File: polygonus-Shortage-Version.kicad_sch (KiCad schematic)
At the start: 10 parts, among them J1 Conn_01x01, J2 Conn_01x01, J3 Conn_01x01, J4 Conn_01x32, J5 Conn_01x32, J6 Conn_01x16, J7 Conn_01x16

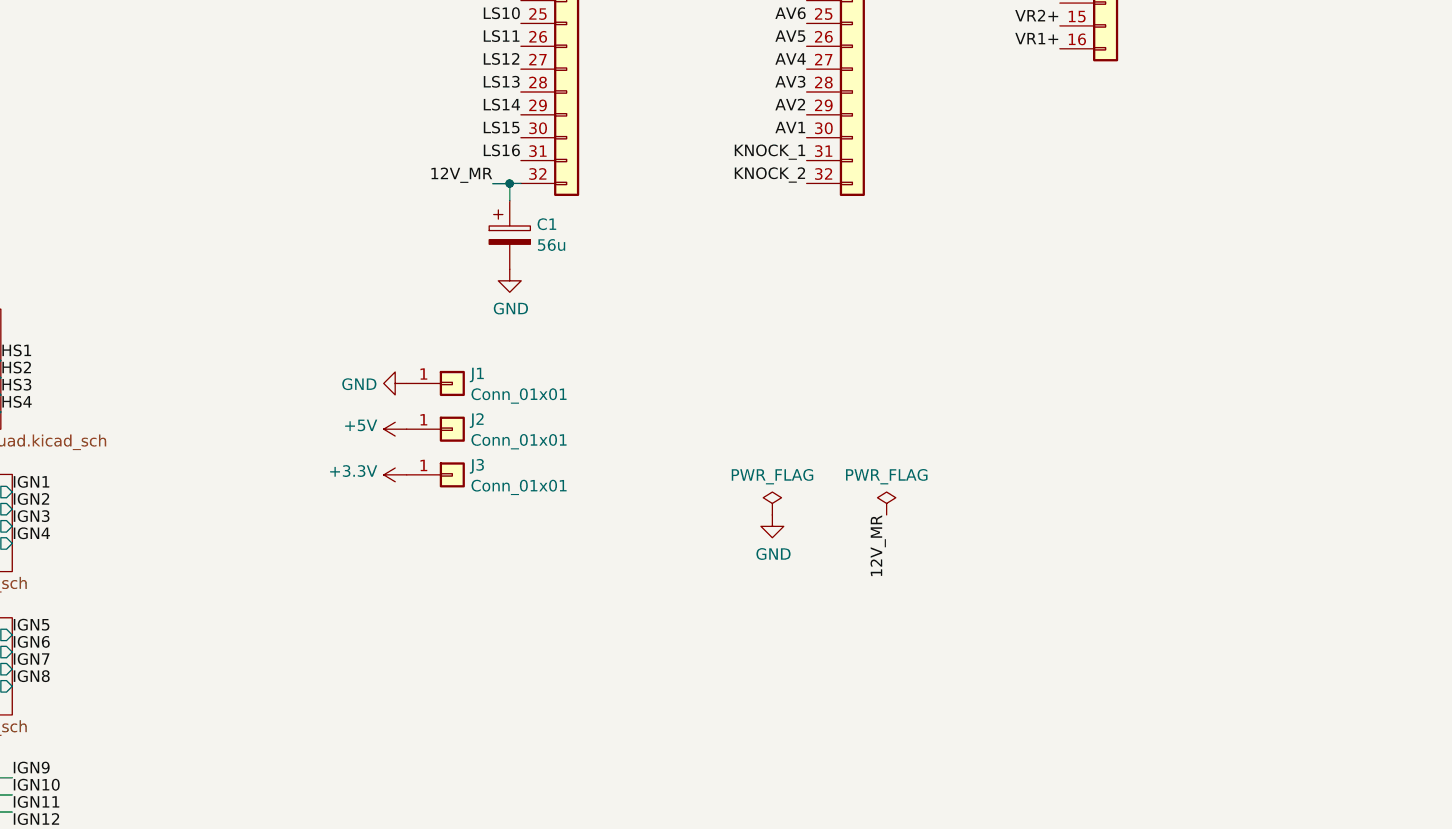
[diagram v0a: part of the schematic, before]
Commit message: added 12v notes to schematic
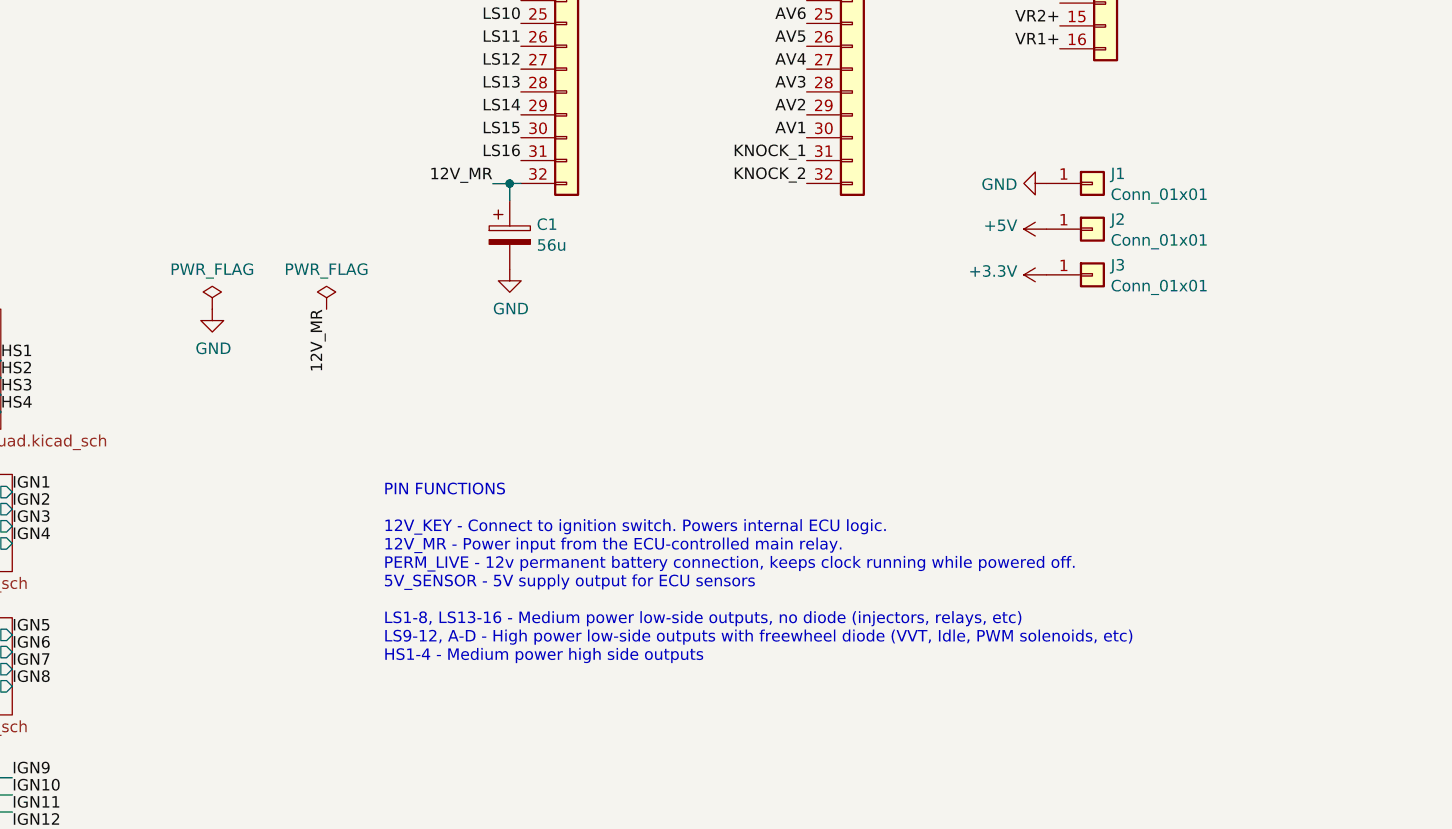
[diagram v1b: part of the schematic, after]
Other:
- note added: "PIN FUNCTIONS 12V_KEY - Connect to ignition switch. Powers internal ECU logic. 12V_MR - Power input from the ECU-controlled main relay. PERM_LIVE - 12v permanent battery connection, keeps clock running while powered off. 5V_SENSOR - 5V supply output for ECU sensors LS1-8, LS13-16 - Medium power low-side outputs, no diode (injectors, relays, etc) LS9-12, A-D - High power low-side outputs with free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"
- moved on the sheet: J1, J2, J3

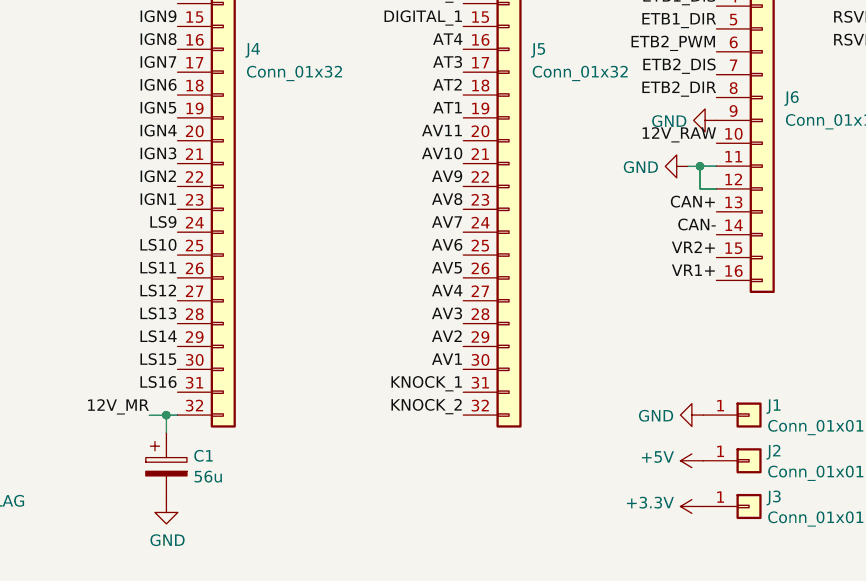
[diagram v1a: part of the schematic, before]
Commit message: Published 1.5 gerbs, bom, cpl and pdf
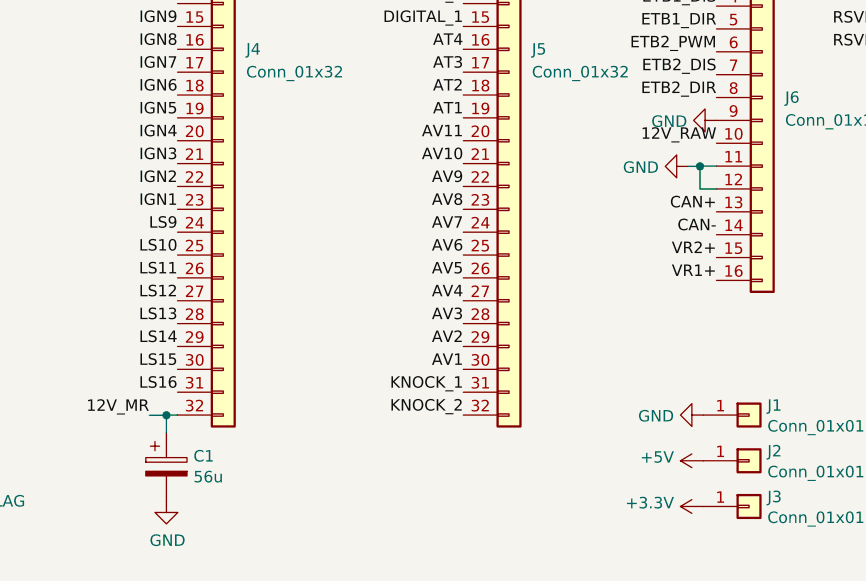
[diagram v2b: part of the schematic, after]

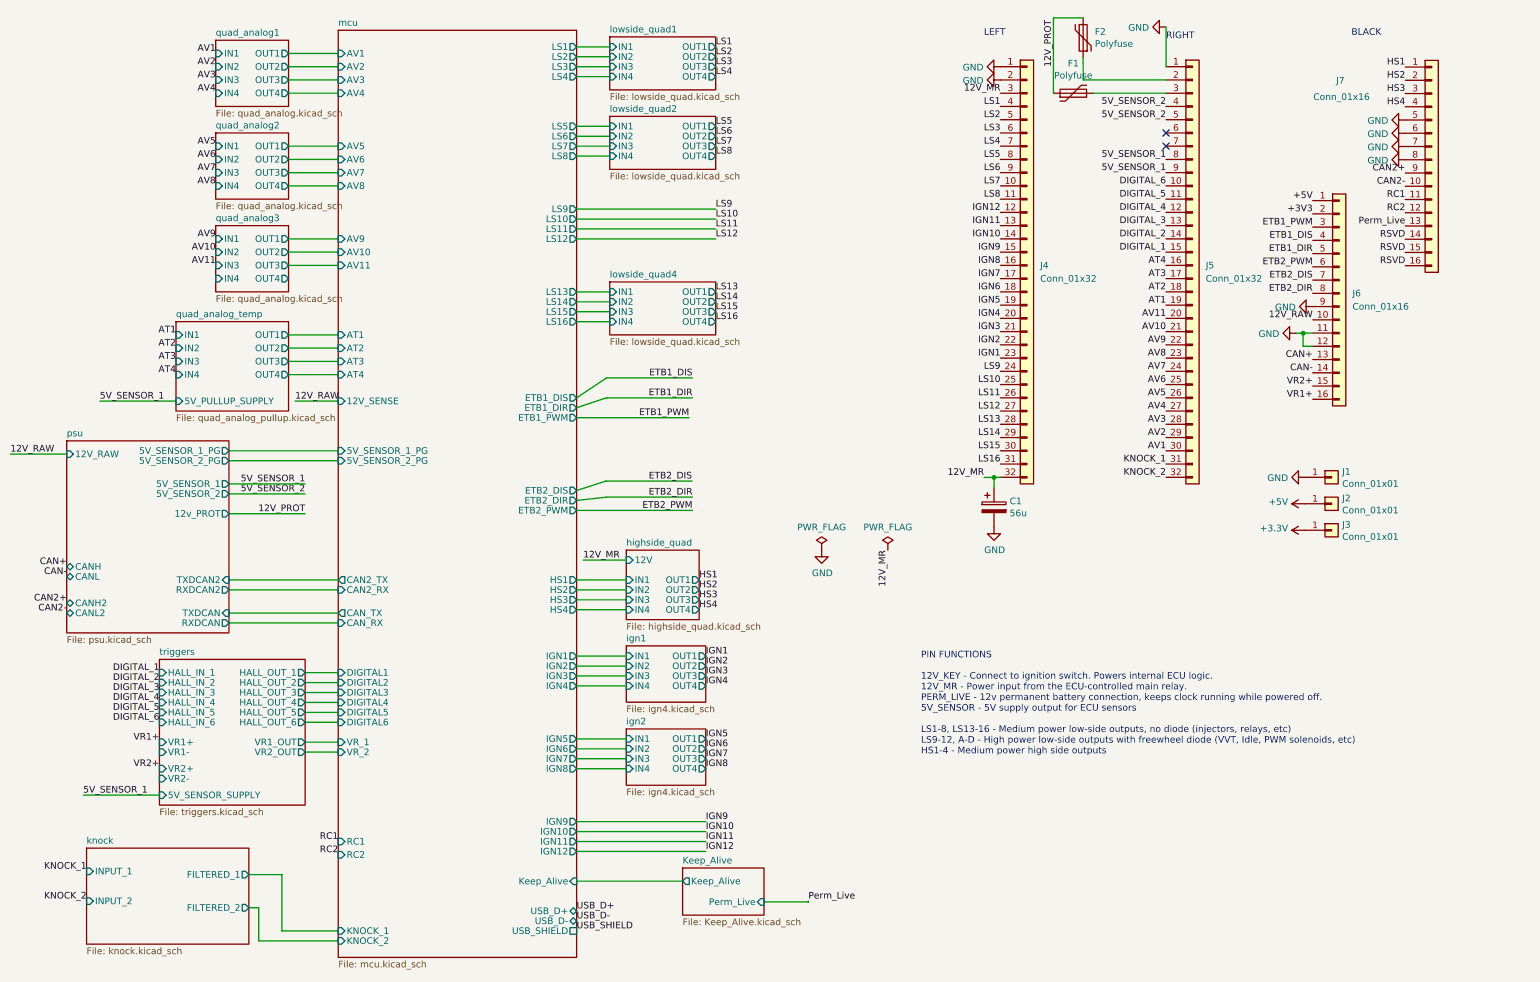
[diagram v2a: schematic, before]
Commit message: make hardware updates: - fix erc/drc errors - switch to VNLD5090 - switch to SOIC8 ignition drivers - BOM deduplication of similar parts
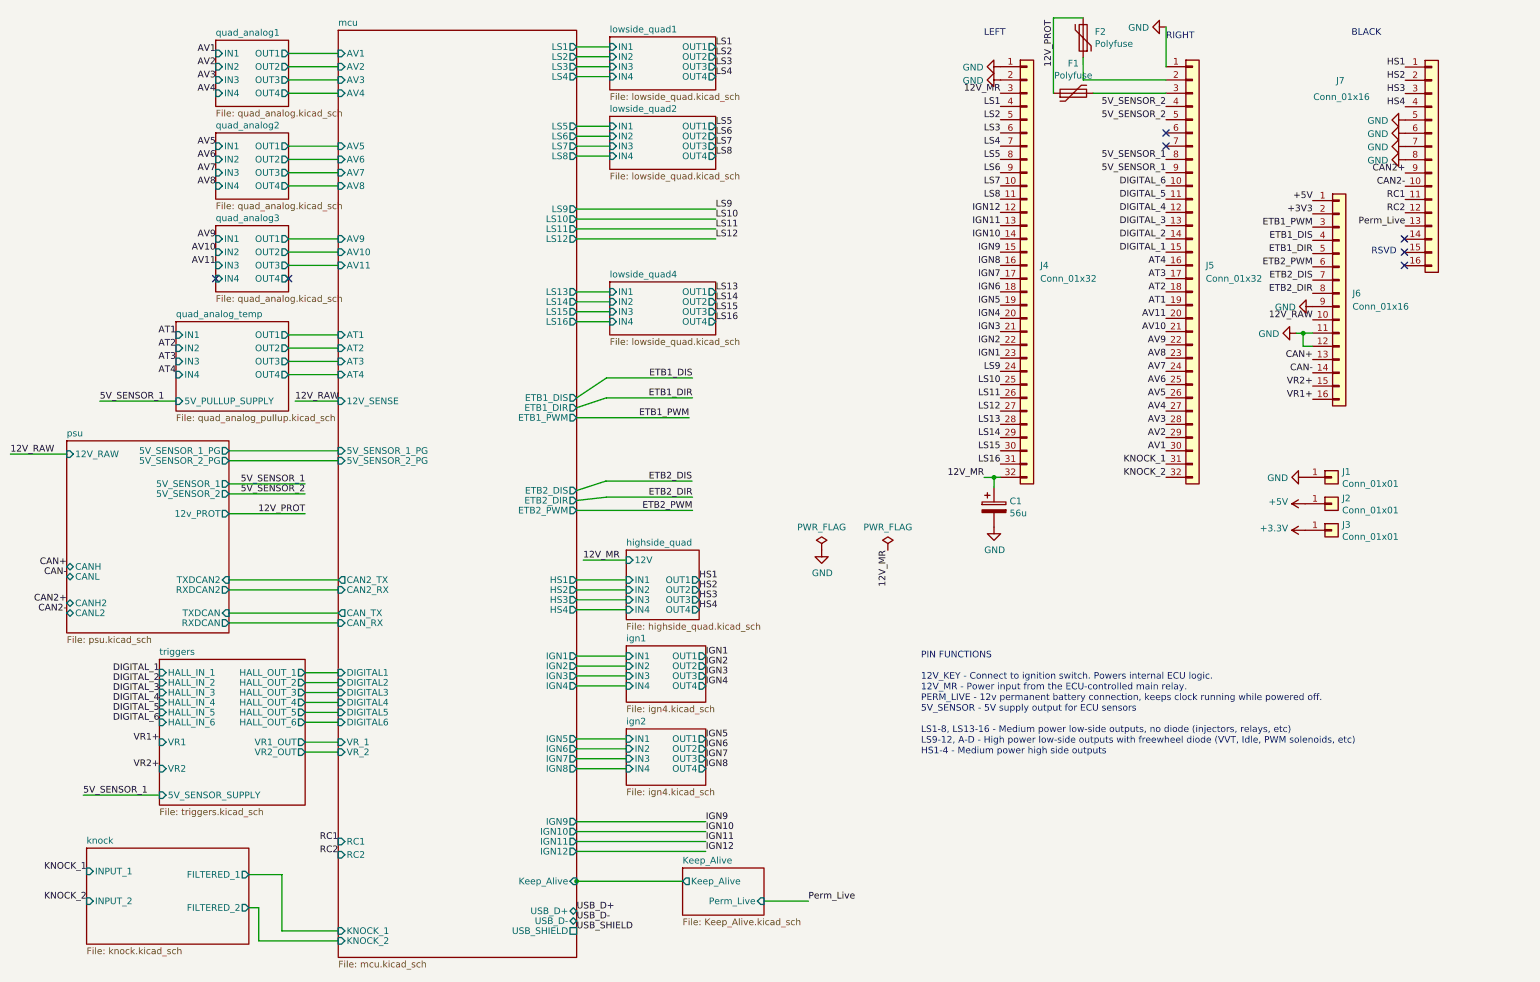
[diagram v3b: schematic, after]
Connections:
- removed net RSVD: J7.14 (Pin_14), J7.15 (Pin_15), J7.16 (Pin_16)
- no-connect marks 2 -> 7
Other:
- sheet triggers ports: added VR1, VR2; removed VR1+, VR1-, VR2+, VR2-
- note added: "RSVD"
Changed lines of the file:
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@@
   (junction (at 253.6325 75.2399) (diameter 0) (color 0 0 0 0)
   )
+  (junction (at 114.3 180.34) (diameter 0) (color 0 0 0 0)
+  )
+  (no_connect (at 45.085 64.77))
+  (no_connect (at 59.055 64.77))
+  (no_connect (at 273.05 59.69))
   (no_connect (at 227.33 36.83))
   (no_connect (at 227.33 39.37))
+  (no_connect (at 273.05 62.23))
+  (no_connect (at 273.05 57.15))
   (wire (pts (xy 62.23 144.145) (xy 68.58 144.145))
     (stroke (width 0) (type default))
   )
-  (wire (pts (xy 150.2316 184.3116) (xy 158.75 184.3116))
+  (wire (pts (xy 150.2316 184.15) (xy 158.75 184.15))
     (stroke (width 0) (type default))
   )
@@
     (stroke (width 0) (type default))
   )
-  (wire (pts (xy 134.62 180.325) (xy 114.3 180.325))
-    (stroke (width 0) (type default))
-  )
   (wire (pts (xy 68.58 59.69) (xy 59.055 59.69))
     (stroke (width 0) (type default))
@@
     (stroke (width 0) (type default))
   )
-  (wire (pts (xy 158.75 184.3116) (xy 158.75 184.15))
-    (stroke (width 0) (type default))
-  )
   (wire (pts (xy 59.055 62.23) (xy 68.58 62.23))
     (stroke (width 0) (type default))
@@
     (stroke (width 0) (type default))
   )
+  (wire (pts (xy 114.3 180.34) (xy 134.62 180.34))
+    (stroke (width 0) (type default))
+  )
   (wire (pts (xy 120.015 87.63) (xy 136.525 87.63))
     (stroke (width 0) (type default))
@@
   )
   (text "LEFT" (at 192.405 18.415 0)
+    (effects (font (size 1.27 1.27)) (justify left bottom))
+  )
+  (text "RSVD" (at 266.7 60.325 0)
     (effects (font (size 1.27 1.27)) (justify left bottom))
   )
@@
     (effects (font (size 1.27 1.27)) (justify right bottom))
   )
-  (label "RSVD" (at 273.2114 57.2119 180) (fields_autoplaced)
-    (effects (font (size 1.27 1.27)) (justify right bottom))
-  )
   (label "ETB2_DIS" (at 255.4645 65.0496 180) (fields_autoplaced)
     (effects (font (size 1.27 1.27)) (justify right bottom))
@@
     (effects (font (size 1.27 1.27)) (justify right bottom))
   )
-  (label "RSVD" (at 273.2114 62.2919 180) (fields_autoplaced)
-    (effects (font (size 1.27 1.27)) (justify right bottom))
-  )
   (label "LS6" (at 140.97 37.465 0) (fields_autoplaced)
     (effects (font (size 1.27 1.27)) (justify left bottom))
@@
   (label "LS14" (at 140.97 69.215 0) (fields_autoplaced)
     (effects (font (size 1.27 1.27)) (justify left bottom))
-  )
-  (label "RSVD" (at 273.2114 59.7519 180) (fields_autoplaced)
-    (effects (font (size 1.27 1.27)) (justify right bottom))
   )
   (label "HS4" (at 273.2114 31.8119 180) (fields_autoplaced)
@@
       (effects (font (size 1.27 1.27)) (justify left))
     )
+    (pin "OUT1" output (at 59.055 57.15 0)
+      (effects (font (size 1.27 1.27)) (justify right))
+    )
+    (pin "OUT2" output (at 59.055 59.69 0)
+      (effects (font (size 1.27 1.27)) (justify right))
+    )
+    (pin "OUT3" output (at 59.055 62.23 0)
+      (effects (font (size 1.27 1.27)) (justify right))
+    )
     (pin "IN4" input (at 45.085 64.77 180)
       (effects (font (size 1.27 1.27)) (justify left))
-    )
-    (pin "OUT1" output (at 59.055 57.15 0)
-      (effects (font (size 1.27 1.27)) (justify right))
-    )
-    (pin "OUT2" output (at 59.055 59.69 0)
-      (effects (font (size 1.27 1.27)) (justify right))
-    )
-    (pin "OUT3" output (at 59.055 62.23 0)
-      (effects (font (size 1.27 1.27)) (justify right))
     )
     (pin "OUT4" output (at 59.055 64.77 0)
@@
       (effects (font (size 1.27 1.27)) (justify right))
     )
-    (pin "VR1+" input (at 34.29 153.67 180)
-      (effects (font (size 1.27 1.27)) (justify left))
-    )
-    (pin "VR1-" input (at 34.29 155.575 180)
-      (effects (font (size 1.27 1.27)) (justify left))
-    )
-    (pin "VR2+" input (at 34.29 158.75 180)
-      (effects (font (size 1.27 1.27)) (justify left))
-    )
-    (pin "VR2-" input (at 34.29 160.655 180)
+    (pin "VR1" input (at 34.29 153.67 180)
+      (effects (font (size 1.27 1.27)) (justify left))
+    )
+    (pin "VR2" input (at 34.29 158.75 180)
       (effects (font (size 1.27 1.27)) (justify left))
     )
@@
       (effects (font (size 1.27 1.27)) (justify left top))
     )
-    (pin "Perm_Live" input (at 150.2316 184.3116 0)
-      (effects (font (size 1.27 1.27)) (justify right))
-    )
-    (pin "Keep_Alive" output (at 134.62 180.325 180)
-      (effects (font (size 1.27 1.27)) (justify left))
-    )
+    (pin "Perm_Live" input (at 150.2316 184.15 0)
+      (effects (font (size 1.27 1.27)) (justify right))
+    )
+    (pin "Keep_Alive" output (at 134.62 180.34 180)
+      (effects (font (size 1.27 1.27)) (justify left))
+    )
